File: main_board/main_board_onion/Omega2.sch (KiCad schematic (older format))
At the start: 23 parts, among them J10 RJ45, J11 USB_B_Micro_Omega, Q1 BSS138, U3 H1102, U4 CP2102N-A01-GQFN24

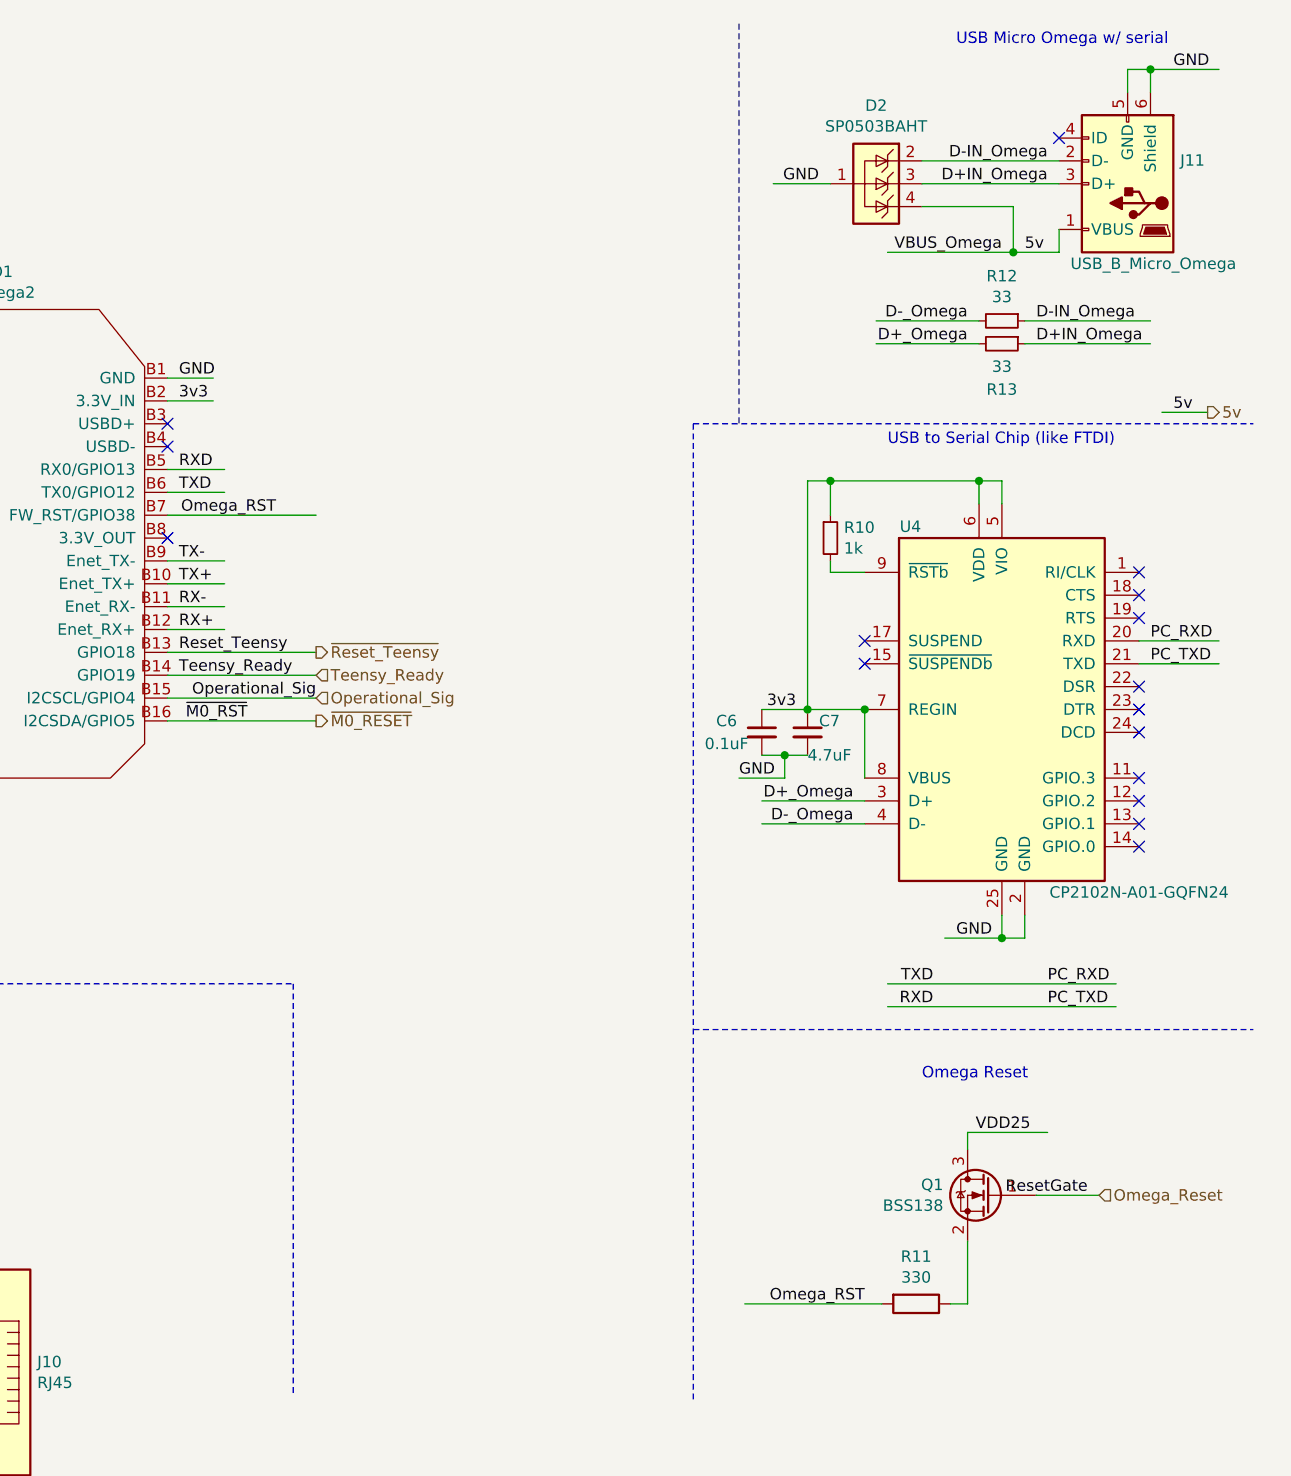
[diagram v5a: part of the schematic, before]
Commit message: went back to original Macrofab v2 files and made changes for v3.5
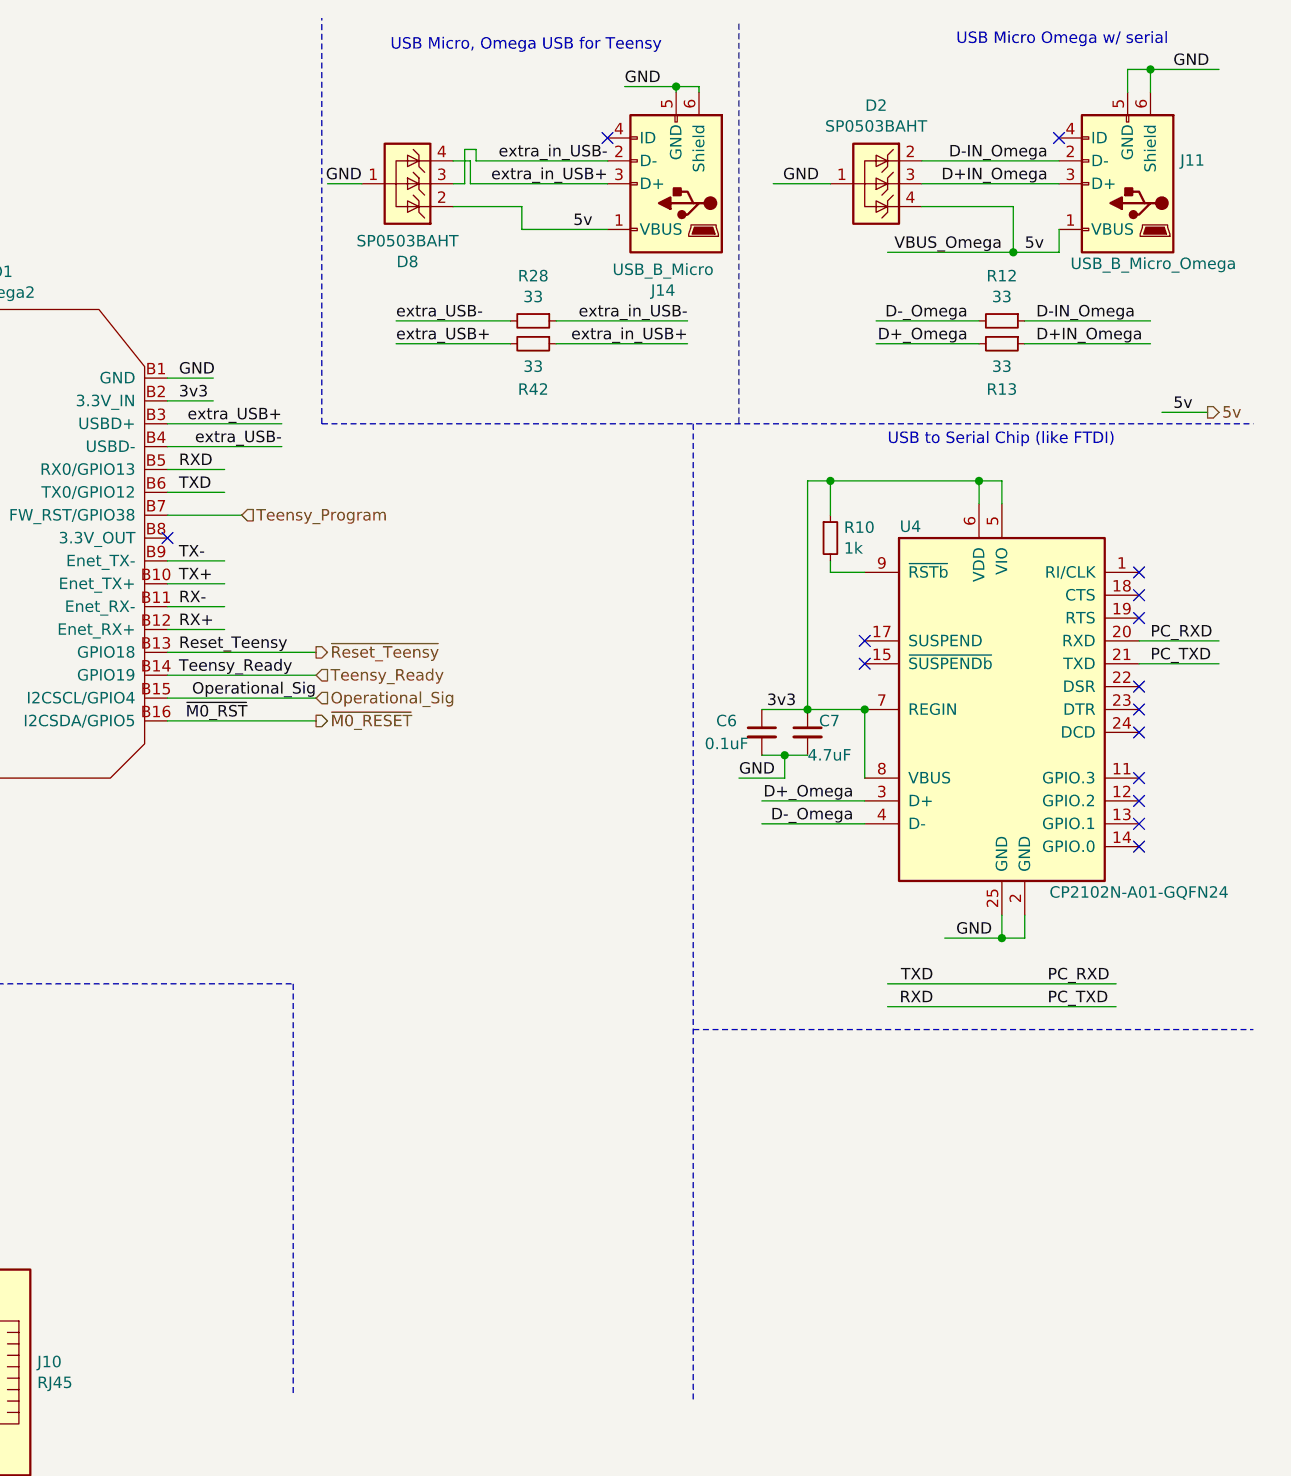
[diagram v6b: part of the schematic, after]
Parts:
- removed Q1: BSS138, Package_TO_SOT_SMD:SOT-23, symbol Transistor_FET:BSS138
- removed R11: 330, Resistor_SMD:R_0603_1608Metric, symbol Device:R
- added D8: SP0503BAHT, Package_TO_SOT_SMD:SOT-143, symbol main_board_onion-rescue:SP0503BAHT-Power_Protection
- added J14: USB_B_Micro, molex_105133:MOLEX_105133-0001_0, symbol Connector:USB_B_Micro
- added R28, R42: 33, Resistor_SMD:R_0603_1608Metric, symbol Device:R_Small
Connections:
- net labels added: Teensy_Program, extra_USB+, extra_USB-, extra_in_USB+, extra_in_USB-
- net labels removed: Omega_RST, Omega_Reset, ResetGate
- wire segments 120 -> 136
- no-connect marks 36 -> 35
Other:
- note added: "USB Micro, Omega USB for Teensy"
- note removed: "Omega Reset\n"
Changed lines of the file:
@@
-EESchema Schematic File Version 5
+EESchema Schematic File Version 4
 LIBS:main_board_onion-cache
-EELAYER 29 0
+EELAYER 30 0
 EELAYER END
 $Descr A4 11693 8268
@@
 Wire Wire Line
 	5000 2050 4800 2050
-Text Label 6925 2650 2    50   ~ 0
-Omega_RST
-NoConn ~ 6450 2250
-NoConn ~ 6450 2350
 NoConn ~ 6450 2750
 NoConn ~ 5000 3550
@@
 NoConn ~ 5000 3350
 NoConn ~ 5000 3450
-Wire Wire Line
-	6450 2650 7100 2650
 Text HLabel 7100 3350 2    50   Input ~ 0
 Teensy_Ready
@@
 Text Label 4950 2150 2    50   ~ 0
 VDD25
-Wire Wire Line
-	9575 6100 8975 6100
-Wire Wire Line
-	9950 5425 9950 5350
-Wire Wire Line
-	9950 5350 10300 5350
-Wire Wire Line
-	9875 6100 9950 6100
-Wire Wire Line
-	9950 6100 9950 5825
-$Comp
-L Device:R R11
-U 1 1 5D0274A7
-P 9725 6100
-F 0 "R11" V 9518 6100 50  0000 C CNN
-F 1 "330" V 9609 6100 50  0000 C CNN
-F 2 "Resistor_SMD:R_0603_1608Metric" V 9655 6100 50  0001 C CNN
-F 3 "~" H 9725 6100 50  0001 C CNN
-	1    9725 6100
-	0    1    1    0
-$EndComp
-$Comp
-L Transistor_FET:BSS138 Q1
-U 1 1 5D02392E
-P 10050 5625
-F 0 "Q1" H 10256 5671 50  0000 L CNN
-F 1 "BSS138" H 10256 5580 50  0000 L CNN
-F 2 "Package_TO_SOT_SMD:SOT-23" H 10250 5550 50  0001 L CIN
-F 3 "https://www.fairchildsemi.com/datasheets/BS/BSS138.pdf" H 10050 5625 50  0001 L CNN
-	1    10050 5625
-	-1   0    0    -1
-$EndComp
-Text Label 9500 6100 2    50   ~ 0
-Omega_RST
-Wire Wire Line
-	10250 5625 10525 5625
-Text Label 10225 5350 2    50   ~ 0
-VDD25
-Text HLabel 10525 5625 2    50   Input ~ 0
-Omega_Reset
-Text Label 10475 5625 2    50   ~ 0
-ResetGate
 Text Label 6800 3550 2    50   ~ 0
 ~M0_RST
@@
 NoConn ~ 2450 7100
 Wire Notes Line
-	8750 2250 11200 2250
-Text Notes 9750 5125 0    50   ~ 0
-Omega Reset\n
-Wire Notes Line
 	8750 2250 8750 6525
 NoConn ~ 5000 2450
 NoConn ~ 5000 2550
 NoConn ~ 5000 2650
+Text Label 6950 2250 2    50   ~ 0
+extra_USB+
+Text Label 6950 2350 2    50   ~ 0
+extra_USB-
+Wire Wire Line
+	6450 2250 6950 2250
+Wire Wire Line
+	6450 2350 6950 2350
+Wire Wire Line
+	8775 775  8675 775
+Text Label 7450 1800 0    50   ~ 0
+extra_USB-
+Wire Wire Line
+	7950 1900 7450 1900
+Wire Wire Line
+	8775 800  8775 775
+Wire Wire Line
+	7950 1800 7450 1800
+Wire Wire Line
+	8675 775  8450 775
+Text Label 8450 775  0    50   ~ 0
+GND
+Wire Wire Line
+	8675 800  8675 775
+Text Label 7450 1900 0    50   ~ 0
+extra_USB+
+Connection ~ 8675 775
+NoConn ~ 8375 1000
+$Comp
+L Device:R_Small R28
+U 1 1 5D7FF1F9
+P 8050 1800
+F 0 "R28" V 7854 1800 50  0000 C CNN
+F 1 "33" V 7945 1800 50  0000 C CNN
+F 2 "Resistor_SMD:R_0603_1608Metric" H 8050 1800 50  0001 C CNN
+F 3 "~" H 8050 1800 50  0001 C CNN
+	1    8050 1800
+	0    1    1    0
+$EndComp
+$Comp
+L Device:R_Small R42
+U 1 1 5D7FF20A
+P 8050 1900
+F 0 "R42" V 8250 1900 50  0000 C CNN
+F 1 "33" V 8150 1900 50  0000 C CNN
+F 2 "Resistor_SMD:R_0603_1608Metric" H 8050 1900 50  0001 C CNN
+F 3 "~" H 8050 1900 50  0001 C CNN
+	1    8050 1900
+	0    1    1    0
+$EndComp
+$Comp
+L Connector:USB_B_Micro J14
+U 1 1 5D6FE88E
+P 8675 1200
+F 0 "J14" H 8732 1667 50  0000 C CNN
+F 1 "USB_B_Micro" H 8732 1576 50  0000 C CNN
+F 2 "molex_105133:MOLEX_105133-0001_0" H 8825 1150 50  0001 C CNN
+F 3 "~" H 8825 1150 50  0001 C CNN
+	1    8675 1200
+	-1   0    0    1
+$EndComp
+Text Label 8725 1800 2    50   ~ 0
+extra_in_USB-
+Wire Wire Line
+	8150 1800 8725 1800
+Text Label 8725 1900 2    50   ~ 0
+extra_in_USB+
+Wire Wire Line
+	8150 1900 8725 1900
+Text Label 8375 1100 2    50   ~ 0
+extra_in_USB-
+Text Label 8375 1200 2    50   ~ 0
+extra_in_USB+
+Wire Wire Line
+	7800 1100 8375 1100
+Text Label 8225 1400 0    50   ~ 0
+5v
+Wire Wire Line
+	8375 1400 8000 1400
+Wire Wire Line
+	8000 1400 8000 1300
+Text Notes 7425 625  0    50   ~ 0
+USB Micro, Omega USB for Teensy
+Wire Notes Line
+	7125 2250 7125 475
+Wire Notes Line
+	7125 2250 11200 2250
+$Comp
+L main_board_onion-rescue:SP0503BAHT-Power_Protection D8
+U 1 1 5D7FF1E2
+P 7500 1200
+F 0 "D8" V 7158 1200 50  0000 C CNN
+F 1 "SP0503BAHT" V 7249 1200 50  0000 C CNN
+F 2 "Package_TO_SOT_SMD:SOT-143" H 7725 1150 50  0001 L CNN
+F 3 "http://www.littelfuse.com/~/media/files/littelfuse/technical%20resources/documents/data%20sheets/sp05xxba.pdf" H 7625 1325 50  0001 C CNN
+	1    7500 1200
+	0    1    -1   0
+$EndComp
+Text Label 7300 1200 2    50   ~ 0
+GND
+Wire Wire Line
+	7300 1200 7150 1200
+Wire Wire Line
+	7775 1200 7775 1100
+Wire Wire Line
+	7775 1100 7700 1100
+Wire Wire Line
+	7775 1200 8375 1200
+Wire Wire Line
+	7800 1100 7800 1050
+Wire Wire Line
+	7800 1050 7750 1050
+Wire Wire Line
+	7750 1050 7750 1200
+Wire Wire Line
+	7750 1200 7700 1200
+Wire Wire Line
+	7700 1300 8000 1300
+Text HLabel 6775 2650 2    50   Input ~ 0
+Teensy_Program
+Wire Wire Line
+	6450 2650 6775 2650
 $EndSCHEMATC
